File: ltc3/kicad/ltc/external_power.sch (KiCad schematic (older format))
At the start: 46 parts, among them IC701 TLP3542, IC702 TLP3542, IC703 TLP3542, IC704 TLP3542, M701 W28-XQ1A-1, M702 W28-XQ1A-1, M703 W28-XQ1A-1, M704 W28-XQ1A-1, P701 43045-1000, P702 43025-1000, P703 43045-0800, P704 43025-0800, P705 43045-0800, P706 43025-0800, P707 1327G6, P708 1327, P709 1327G6, P710 1327, P711 1327G6, P712 1327, P713 1327G6, P714 1327, Q701 PMV45EN, Q702 PMV45EN, Q703 PMV45EN, Q704 PMV45EN, SW701 SP3T, SW702 SP3T, SW703 SP3T, SW704 SP3T

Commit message: LTC3: Split single-board design into two boards.
Separated the charge controller and cell protection circuitry onto its
own board (kicad/charge_controller).  The DC-DC converters,
BeagleBone, external power and triggers, and ignition fire control
circuitry remains together (kicad/ltc).

Both boards have had their schematics updated.  Sub-sheets for
circuitry moved to the other board were removed.  Still more work
remaining, though (e.g., add I2C connectors to Charge Controller
schematic; add battery power connector to LTC board; etc.).

Schematic components were *not* re-annotated to align with new sheet
numbering, as it would screw up the existing layout work (i.e., placed
components would disappear), and that would make us sad engineers.

Both boards have had their PCB layouts converted to four-layer.
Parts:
- M701, M702, M703, M704, P702, P704, P706, P707, P708, P709, P710, P711, P712, P713, P714, SW701, SW702, SW703, SW704: footprint OFF-BOARD -> (none)
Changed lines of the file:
@@
 LIBS:atmel
 LIBS:audio
-LIBS:bbd
 LIBS:brooktre
 LIBS:cmos4000
@@
 LIBS:transistors
 LIBS:ttl_ieee
-LIBS:Launch_Tower_Computer_III-cache
 EELAYER 25 0
 EELAYER END
 $Descr B 17000 11000
 encoding utf-8
-Sheet 7 8
+Sheet 7 6
 Title "LTC3 External Device Power"
 Date "2016-05-09"
@@
 EXT_PWR_EN_1
 $Comp
-L GND #PWR701
+L GND #PWR081
 U 1 1 557E02AD
 P 1650 4100
-F 0 "#PWR701" H 1650 4100 30  0001 C CNN
+F 0 "#PWR081" H 1650 4100 30  0001 C CNN
 F 1 "GND" H 1650 4030 30  0001 C CNN
 F 2 "" H 1650 4100 60  0000 C CNN
@@
 $EndComp
 $Comp
-L GND #PWR705
+L GND #PWR082
 U 1 1 557E02DD
 P 3900 3800
-F 0 "#PWR705" H 3900 3800 30  0001 C CNN
+F 0 "#PWR082" H 3900 3800 30  0001 C CNN
 F 1 "GND" H 3900 3730 30  0001 C CNN
 F 2 "" H 3900 3800 60  0000 C CNN
@@
 $EndComp
 $Comp
-L +5V #PWR703
+L +5V #PWR083
 U 1 1 56544A2B
 P 2450 2250
-F 0 "#PWR703" H 2450 2100 50  0001 C CNN
+F 0 "#PWR083" H 2450 2100 50  0001 C CNN
 F 1 "+5V" H 2450 2390 50  0000 C CNN
 F 2 "" H 2450 2250 60  0000 C CNN
@@
 EXT_PWR_EN_2
 $Comp
-L GND #PWR707
+L GND #PWR084
 U 1 1 56CA75BB
 P 6850 4100
-F 0 "#PWR707" H 6850 4100 30  0001 C CNN
+F 0 "#PWR084" H 6850 4100 30  0001 C CNN
 F 1 "GND" H 6850 4030 30  0001 C CNN
 F 2 "" H 6850 4100 60  0000 C CNN
@@
 $EndComp
 $Comp
-L GND #PWR711
+L GND #PWR085
 U 1 1 56CA75CD
 P 9100 3800
-F 0 "#PWR711" H 9100 3800 30  0001 C CNN
+F 0 "#PWR085" H 9100 3800 30  0001 C CNN
 F 1 "GND" H 9100 3730 30  0001 C CNN
 F 2 "" H 9100 3800 60  0000 C CNN
@@
 $EndComp
 $Comp
-L +5V #PWR709
+L +5V #PWR086
 U 1 1 56CA760C
 P 7650 2250
-F 0 "#PWR709" H 7650 2100 50  0001 C CNN
+F 0 "#PWR086" H 7650 2100 50  0001 C CNN
 F 1 "+5V" H 7650 2390 50  0000 C CNN
 F 2 "" H 7650 2250 60  0000 C CNN
@@
 $EndComp
 $Comp
-L +12V #PWR714
+L +12V #PWR087
 U 1 1 56CA7612
 P 12500 4150
-F 0 "#PWR714" H 12500 4000 50  0001 C CNN
+F 0 "#PWR087" H 12500 4000 50  0001 C CNN
 F 1 "+12V" H 12500 4290 50  0000 C CNN
 F 2 "" H 12500 4150 60  0000 C CNN
@@
 EXT_PWR_EN_3
 $Comp
-L GND #PWR702
+L GND #PWR088
 U 1 1 56CA9336
 P 1650 10100
-F 0 "#PWR702" H 1650 10100 30  0001 C CNN
+F 0 "#PWR088" H 1650 10100 30  0001 C CNN
 F 1 "GND" H 1650 10030 30  0001 C CNN
 F 2 "" H 1650 10100 60  0000 C CNN
@@
 $EndComp
 $Comp
-L +5V #PWR704
+L +5V #PWR089
 U 1 1 56CA9387
 P 2450 8250
-F 0 "#PWR704" H 2450 8100 50  0001 C CNN
+F 0 "#PWR089" H 2450 8100 50  0001 C CNN
 F 1 "+5V" H 2450 8390 50  0000 C CNN
 F 2 "" H 2450 8250 60  0000 C CNN
@@
 EXT_PWR_EN_4
 $Comp
-L GND #PWR708
+L GND #PWR090
 U 1 1 56CA93AD
 P 6850 10100
-F 0 "#PWR708" H 6850 10100 30  0001 C CNN
+F 0 "#PWR090" H 6850 10100 30  0001 C CNN
 F 1 "GND" H 6850 10030 30  0001 C CNN
 F 2 "" H 6850 10100 60  0000 C CNN
@@
 $EndComp
 $Comp
-L GND #PWR712
+L GND #PWR091
 U 1 1 56CA93BF
 P 9100 9800
-F 0 "#PWR712" H 9100 9800 30  0001 C CNN
+F 0 "#PWR091" H 9100 9800 30  0001 C CNN
 F 1 "GND" H 9100 9730 30  0001 C CNN
 F 2 "" H 9100 9800 60  0000 C CNN
@@
 $EndComp
 $Comp
-L +5V #PWR710
+L +5V #PWR092
 U 1 1 56CA93FE
 P 7650 8250
-F 0 "#PWR710" H 7650 8100 50  0001 C CNN
+F 0 "#PWR092" H 7650 8100 50  0001 C CNN
 F 1 "+5V" H 7650 8390 50  0000 C CNN
 F 2 "" H 7650 8250 60  0000 C CNN
@@
 F 0 "P706" H 13700 5150 50  0000 L CNN
 F 1 "43025-0800" V 13800 4250 50  0000 L CNN
-F 2 "OFF-BOARD" H 13700 4650 50  0001 C CNN
+F 2 "" H 13700 4650 50  0001 C CNN
 F 3 "" H 13700 4650 50  0000 C CNN
 F 4 "MicroFit3 2x4 recept." V 13900 4650 50  0000 C CNN "Note"
@@
 F 0 "M703" H 15450 5425 50  0000 C CNN
 F 1 "W28-XQ1A-1" H 15450 5225 50  0000 C CNN
-F 2 "OFF-BOARD" H 15450 5300 50  0001 C CNN
+F 2 "" H 15450 5300 50  0001 C CNN
 F 3 "" H 15450 5300 50  0000 C CNN
 	1    15450 5300
@@
 F 0 "M704" H 15850 5425 50  0000 C CNN
 F 1 "W28-XQ1A-1" H 15850 5225 50  0000 C CNN
-F 2 "OFF-BOARD" H 15850 5300 50  0001 C CNN
+F 2 "" H 15850 5300 50  0001 C CNN
 F 3 "" H 15850 5300 50  0000 C CNN
 	1    15850 5300
@@
 F 0 "M701" H 14650 5425 50  0000 C CNN
 F 1 "W28-XQ1A-1" H 14650 5225 50  0000 C CNN
-F 2 "OFF-BOARD" H 14650 5300 50  0001 C CNN
+F 2 "" H 14650 5300 50  0001 C CNN
 F 3 "" H 14650 5300 50  0000 C CNN
 	1    14650 5300
@@
 F 0 "M702" H 15050 5425 50  0000 C CNN
 F 1 "W28-XQ1A-1" H 15050 5225 50  0000 C CNN
-F 2 "OFF-BOARD" H 15050 5300 50  0001 C CNN
+F 2 "" H 15050 5300 50  0001 C CNN
 F 3 "" H 15050 5300 50  0000 C CNN
 	1    15050 5300
@@
 Manual Override Switches, Front Panel
 $Comp
-L GND #PWR713
+L GND #PWR093
 U 1 1 56DB5084
 P 11800 2200
-F 0 "#PWR713" H 11800 1950 50  0001 C CNN
+F 0 "#PWR093" H 11800 1950 50  0001 C CNN
 F 1 "GND" H 11808 2026 50  0001 C CNN
 F 2 "" H 11800 2200 50  0000 C CNN
@@
 F 0 "SW701" V 13650 2250 50  0000 R CNN
 F 1 "SP3T" V 13750 2250 50  0000 R CNN
-F 2 "OFF-BOARD" H 13125 2475 50  0001 C CNN
+F 2 "" H 13125 2475 50  0001 C CNN
 F 3 "" H 13125 2475 50  0000 C CNN
 	1    13750 2300
@@
 F 0 "P702" H 13000 2150 50  0000 L CNN
 F 1 "43025-1000" V 13100 1100 50  0000 L CNN
-F 2 "OFF-BOARD" H 13000 1600 50  0001 C CNN
+F 2 "" H 13000 1600 50  0001 C CNN
 F 3 "" H 13000 1600 50  0000 C CNN
 F 4 "MicroFit3 2x5 recept." V 13200 1100 50  0000 L CNN "Note"
@@
 F 0 "SW702" V 14300 2250 50  0000 R CNN
 F 1 "SP3T" V 14400 2250 50  0000 R CNN
-F 2 "OFF-BOARD" H 13775 2475 50  0001 C CNN
+F 2 "" H 13775 2475 50  0001 C CNN
 F 3 "" H 13775 2475 50  0000 C CNN
 	1    14400 2300
@@
 F 0 "SW703" V 14950 2250 50  0000 R CNN
 F 1 "SP3T" V 15050 2250 50  0000 R CNN
-F 2 "OFF-BOARD" H 14425 2475 50  0001 C CNN
+F 2 "" H 14425 2475 50  0001 C CNN
 F 3 "" H 14425 2475 50  0000 C CNN
 	1    15050 2300
@@
 F 0 "SW704" V 15600 2250 50  0000 R CNN
 F 1 "SP3T" V 15700 2250 50  0000 R CNN
-F 2 "OFF-BOARD" H 15075 2475 50  0001 C CNN
+F 2 "" H 15075 2475 50  0001 C CNN
 F 3 "" H 15075 2475 50  0000 C CNN
 	1    15700 2300
@@
 F 0 "P704" H 13950 7850 50  0000 L CNN
 F 1 "43025-0800" V 14050 6950 50  0000 L CNN
-F 2 "OFF-BOARD" H 13950 7350 50  0001 C CNN
+F 2 "" H 13950 7350 50  0001 C CNN
 F 3 "" H 13950 7350 50  0000 C CNN
 F 4 "MicroFit3 2x4 recept." V 14150 7350 50  0000 C CNN "Note"
@@
 $EndComp
 $Comp
-L GND #PWR715
+L GND #PWR094
 U 1 1 57141ACA
 P 12850 7850
-F 0 "#PWR715" H 12850 7600 50  0001 C CNN
+F 0 "#PWR094" H 12850 7600 50  0001 C CNN
 F 1 "GND" H 12858 7677 50  0000 C CNN
 F 2 "" H 12850 7850 50  0000 C CNN
@@
 $EndComp
 $Comp
-L GND #PWR706
+L GND #PWR095
 U 1 1 57147239
 P 3900 9800
-F 0 "#PWR706" H 3900 9550 50  0001 C CNN
+F 0 "#PWR095" H 3900 9550 50  0001 C CNN
 F 1 "GND" H 3908 9627 50  0000 C CNN
 F 2 "" H 3900 9800 50  0000 C CNN
@@
 F 0 "P707" H 14750 8150 50  0000 L CNN
 F 1 "1327G6" H 14900 8150 50  0001 C CNN
-F 2 "OFF-BOARD" H 14650 8150 50  0001 C CNN
+F 2 "" H 14650 8150 50  0001 C CNN
 F 3 "" H 14650 8150 50  0000 C CNN
 	1    14650 8150
@@
 F 0 "P708" H 14900 8150 50  0000 L CNN
 F 1 "1327" H 15000 8200 50  0001 C CNN
-F 2 "OFF-BOARD" H 14800 8150 50  0001 C CNN
+F 2 "" H 14800 8150 50  0001 C CNN
 F 3 "" H 14800 8150 50  0000 C CNN
 	1    14800 8150
@@
 F 0 "P709" H 15150 8150 50  0000 L CNN
 F 1 "1327G6" H 15300 8150 50  0001 C CNN
-F 2 "OFF-BOARD" H 15050 8150 50  0001 C CNN
+F 2 "" H 15050 8150 50  0001 C CNN
 F 3 "" H 15050 8150 50  0000 C CNN
 	1    15050 8150
@@
 F 0 "P710" H 15300 8150 50  0000 L CNN
 F 1 "1327" H 15450 8250 50  0001 C CNN
-F 2 "OFF-BOARD" H 15200 8150 50  0001 C CNN
+F 2 "" H 15200 8150 50  0001 C CNN
 F 3 "" H 15200 8150 50  0000 C CNN
 	1    15200 8150
@@
 F 0 "P711" H 15550 8150 50  0000 L CNN
 F 1 "1327G6" H 15800 8150 50  0001 C CNN
-F 2 "OFF-BOARD" H 15450 8150 50  0001 C CNN
+F 2 "" H 15450 8150 50  0001 C CNN
 F 3 "" H 15450 8150 50  0000 C CNN
 	1    15450 8150
@@
 F 0 "P712" H 15700 8150 50  0000 L CNN
 F 1 "1327" H 15900 8150 50  0001 C CNN
-F 2 "OFF-BOARD" H 15600 8150 50  0001 C CNN
+F 2 "" H 15600 8150 50  0001 C CNN
 F 3 "" H 15600 8150 50  0000 C CNN
 	1    15600 8150
@@
 F 0 "P713" H 15950 8150 50  0000 L CNN
 F 1 "1327G6" H 16200 8150 50  0001 C CNN
-F 2 "OFF-BOARD" H 15850 8150 50  0001 C CNN
+F 2 "" H 15850 8150 50  0001 C CNN
 F 3 "" H 15850 8150 50  0000 C CNN
 	1    15850 8150
@@
 F 0 "P714" H 16100 8150 50  0000 L CNN
 F 1 "1327" H 16300 8150 50  0001 C CNN
-F 2 "OFF-BOARD" H 16000 8150 50  0001 C CNN
+F 2 "" H 16000 8150 50  0001 C CNN
 F 3 "" H 16000 8150 50  0000 C CNN
 	1    16000 8150

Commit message: LTC3: Updates to LTC schematic.
1. Cleaned up top-level sheet.
2. Added board-to-board connectors for power, I2C.
3. Miscelleneous component part selection/changes.
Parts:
- removed C702, C703, C704: 1μ, Capacitors_SMD:C_0805, symbol C
- removed IC701, IC702, IC703, IC704: TLP3542, Housings_DIP:DIP-6_W7.62mm, symbol TLP3542
- removed M702, M703, M704: W28-XQ1A-1, symbol BREAKER_1P
- removed P701: 43045-1000, Connectors_Molex:Molex_Microfit3_Header_02x05_Angled_43045-100x, symbol CONN_01X10
- removed P702: 43025-1000, symbol CONN_01X10
- removed P703: 43045-0800, Connectors_Molex:Molex_Microfit3_Header_02x04_Angled_43045-080x, symbol CONN_01X08
- removed P704: 43025-0800, symbol CONN_01X08
- removed P709, P711, P713: 1327G6, symbol CONN_01X01
- removed P710, P712, P714: 1327, symbol CONN_01X01
- removed Q702, Q703, Q704: PMV45EN, TO_SOT_Packages_SMD:SOT-23, symbol PMV45EN
- added C502, C503, C504: 1μ, Capacitors_SMD:C_0805, symbol C
- added M502, M503, M504: 1A, symbol BREAKER_1P
- added P501: JST PH header, Connectors_JST:JST_PH_B9B-PH-K_09x2.00mm_Straight, symbol CONN_01X09
- added P502: JST PH housing, ~, symbol CONN_01X09
- added P505: MicroFit header, Connectors_Molex:Molex_Microfit3_Header_02x04_Angled_43045-080x, symbol CONN_01X08
- added P506: MicroFit recept., symbol CONN_01X08
- added P509, P510, P511, P512, P513, P514: PowerPole, symbol CONN_01X01
- added Q502, Q503, Q504: PMV45EN, TO_SOT_Packages_SMD:SOT-23, symbol PMV45EN
- added U501, U502, U503, U504: TLP3542, Housings_DIP:DIP-6_W7.62mm, symbol TLP3542
- C501: renamed from C701; Mfg_Name (none) -> -; Mfg_PN (none) -> -; Note (none) -> -; Spec (none) -> 25V
- M501: renamed from M701; value W28-XQ1A-1 -> 1A; Mfg_Name (none) -> TE; Mfg_PN (none) -> W28-XQ1A-1; Note (none) -> -; Spec (none) -> -
- P503: renamed from P705; value 43045-0800 -> MicroFit header; Mfg_Name (none) -> Molex; Mfg_PN (none) -> 43045-0800; Note MicroFit3 2x4 header -> -
- P504: renamed from P706; value 43025-0800 -> MicroFit recept.; Mfg_Name (none) -> Molex; Mfg_PN (none) -> 43025-0800; Note MicroFit3 2x4 recept. -> -
- P507: renamed from P707; value 1327G6 -> PowerPole; Mfg_Name (none) -> Anderson; Mfg_PN (none) -> 1327G6; Note (none) -> -
- P508: renamed from P708; value 1327 -> PowerPole; Mfg_Name (none) -> Anderson; Mfg_PN (none) -> 1327; Note (none) -> -
- Q501: renamed from Q701; Mfg_Name (none) -> NXP; Mfg_PN (none) -> PMV45EN; Note (none) -> -; Spec (none) -> -
- R501: renamed from R701; Mfg_Name (none) -> -; Mfg_PN (none) -> -; Note (none) -> -; Spec (none) -> -
- R503: renamed from R703; Mfg_Name (none) -> -; Mfg_PN (none) -> -; Note (none) -> -; Spec (none) -> -
- R505: renamed from R705; Mfg_Name (none) -> -; Mfg_PN (none) -> -; Note (none) -> -; Spec (none) -> -
- renumbered R702 to R502, R704 to R504, R706 to R506, R707 to R507, R708 to R508, R709 to R509, R710 to R510, R711 to R511, R712 to R512, SW701 to SW501, SW702 to SW502, SW703 to SW503, SW704 to SW504
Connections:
- net EXT_POW_1_FET_D: now also P501.1 (P1)
- net EXT_POW_1_LED_CATH: now also P501.2 (P2), U501.2
- net EXT_POW_1_OPTO_RELAY_P: now also U501.6
- net EXT_POW_2_FET_D: now also P501.3 (P3), Q502.3 (D)
- net EXT_POW_2_LED_CATH: now also P501.4 (P4), U502.2
- net EXT_POW_2_OPTO_RELAY_P: now also U502.6
- net EXT_POW_3_FET_D: now also P501.5 (P5), Q503.3 (D)
- net EXT_POW_3_LED_CATH: now also P501.6 (P6), U503.2
- net EXT_POW_3_OPTO_RELAY_P: now also U503.6
- net EXT_POW_4_FET_D: now also P501.7 (P7), Q504.3 (D)
- net EXT_POW_4_LED_CATH: now also P501.8 (P8), U504.2
- net EXT_POW_4_OPTO_RELAY_P: now also U504.6
- net EXT_PWR_EN_2: now also Q502.1 (G)
- net EXT_PWR_EN_3: now also Q503.1 (G)
- net EXT_PWR_EN_4: now also Q504.1 (G)
- net GND: now also C502.2, C503.2, C504.2, P501.9 (P9), P505.2 (P2), P505.4 (P4), P505.6 (P6), P505.8 (P8), Q502.2 (S), Q503.2 (S), Q504.2 (S)
- net EXT_PWR_1_OUT: now reaches C501.1, R503.1
- net EXT_PWR_1_OUT: now also P505.1 (P1), U501.4
- net at R501.2: now also U501.1
- net EXT_PWR_2_OUT: now reaches R504.1
- net EXT_PWR_2_OUT: now also C502.1, P505.3 (P3), U502.4
- net at R502.2: now also U502.1
- net EXT_PWR_3_OUT: now reaches R509.1
- net EXT_PWR_3_OUT: now also C503.1, P505.5 (P5), U503.4
- net at R507.2: now also U503.1
- net EXT_PWR_4_OUT: now reaches R510.1
- net EXT_PWR_4_OUT: now also C504.1, P505.7 (P7), U504.4
- net at R508.2: now also U504.1
- net at P504.5 (P5): now also M503.1
- net at P504.6 (P6): now also M503.2
- net at P504.7 (P7): now also M504.1
- net at P504.8 (P8): now also M504.2
- net at P504.3 (P3): now also M502.1
- net at P504.4 (P4): now also M502.2
- net at SW501.1: now also P502.2 (P2)
- net at SW501.3: now also P502.1 (P1)
- net at SW501.4, SW502.4, SW503.4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: now also P502.9 (P9)
- net at SW502.3: now also P502.3 (P3)
- net at SW502.1: now also P502.4 (P4)
- net at SW503.3: now also P502.5 (P5)
- net at SW503.1: now also P502.6 (P6)
- net at SW504.3: now also P502.7 (P7)
- net at SW504.1: now also P502.8 (P8)
- net at P508.1 (P1): now also P506.7 (P7)
- net at P507.1 (P1): now also P506.8 (P8)
- new net: P506.1 (P1), P514.1 (P1)
- new net: P506.2 (P2), P513.1 (P1)
- new net: P506.3 (P3), P512.1 (P1)
- new net: P506.4 (P4), P511.1 (P1)
- new net: P506.5 (P5), P510.1 (P1)
- new net: P506.6 (P6), P509.1 (P1)
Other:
- note removed: "12V: 1327 (red)\ngnd: 1327G6 (black)"
- moved on the sheet: P507, P508

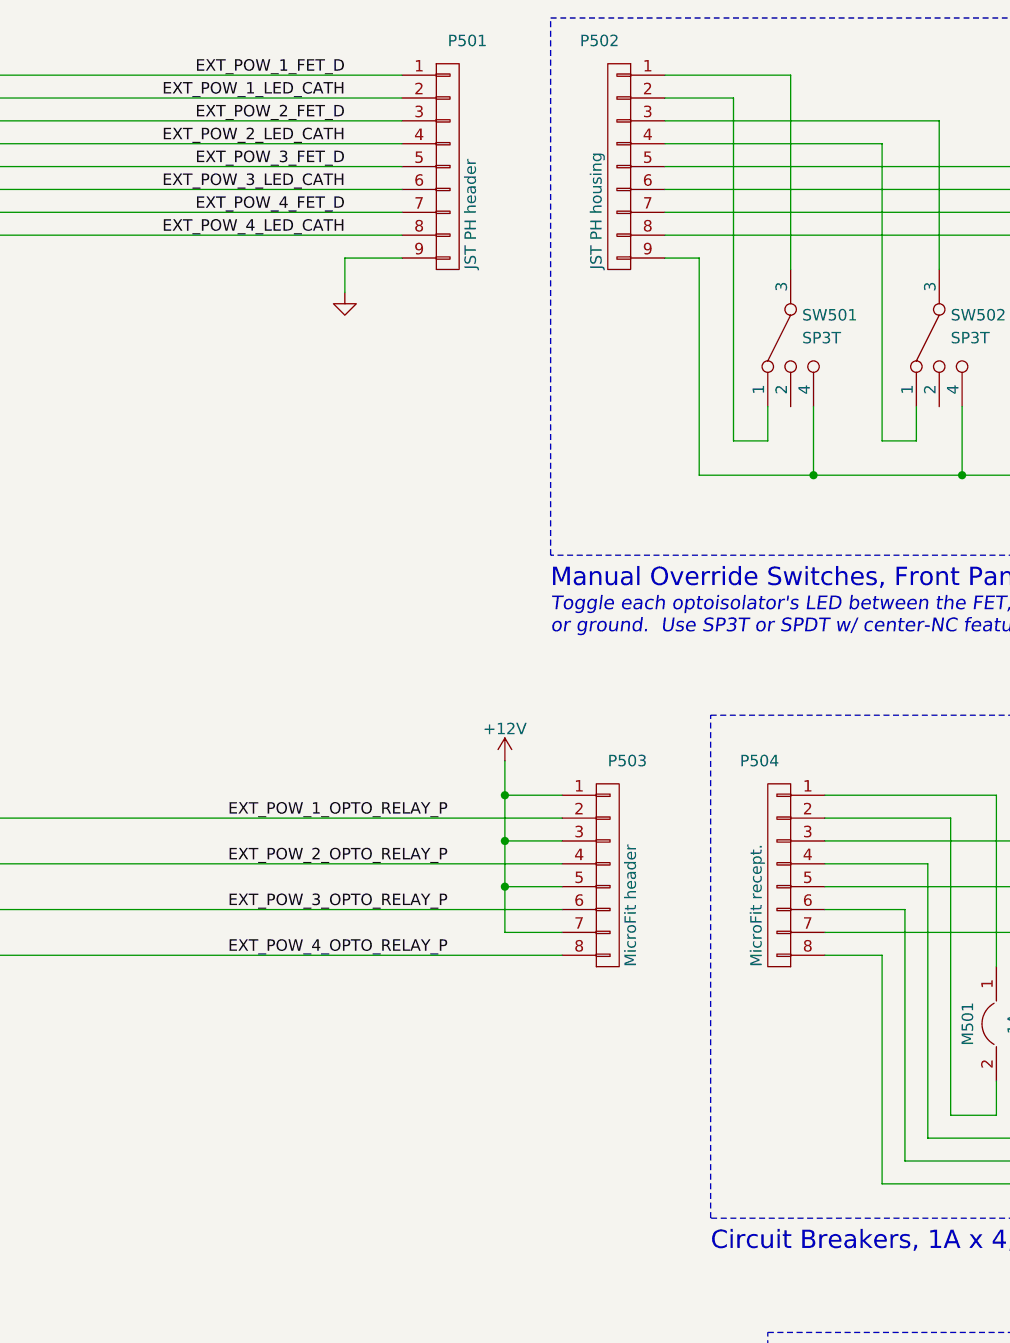
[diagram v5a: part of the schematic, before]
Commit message: LTC3: More BOM work, mostly on the LTC proper.
Plus a few minor tweaks to the charge controller and cell protection
BOMs that should not impact PCB layout.

Nearly finished with LTC BOM.
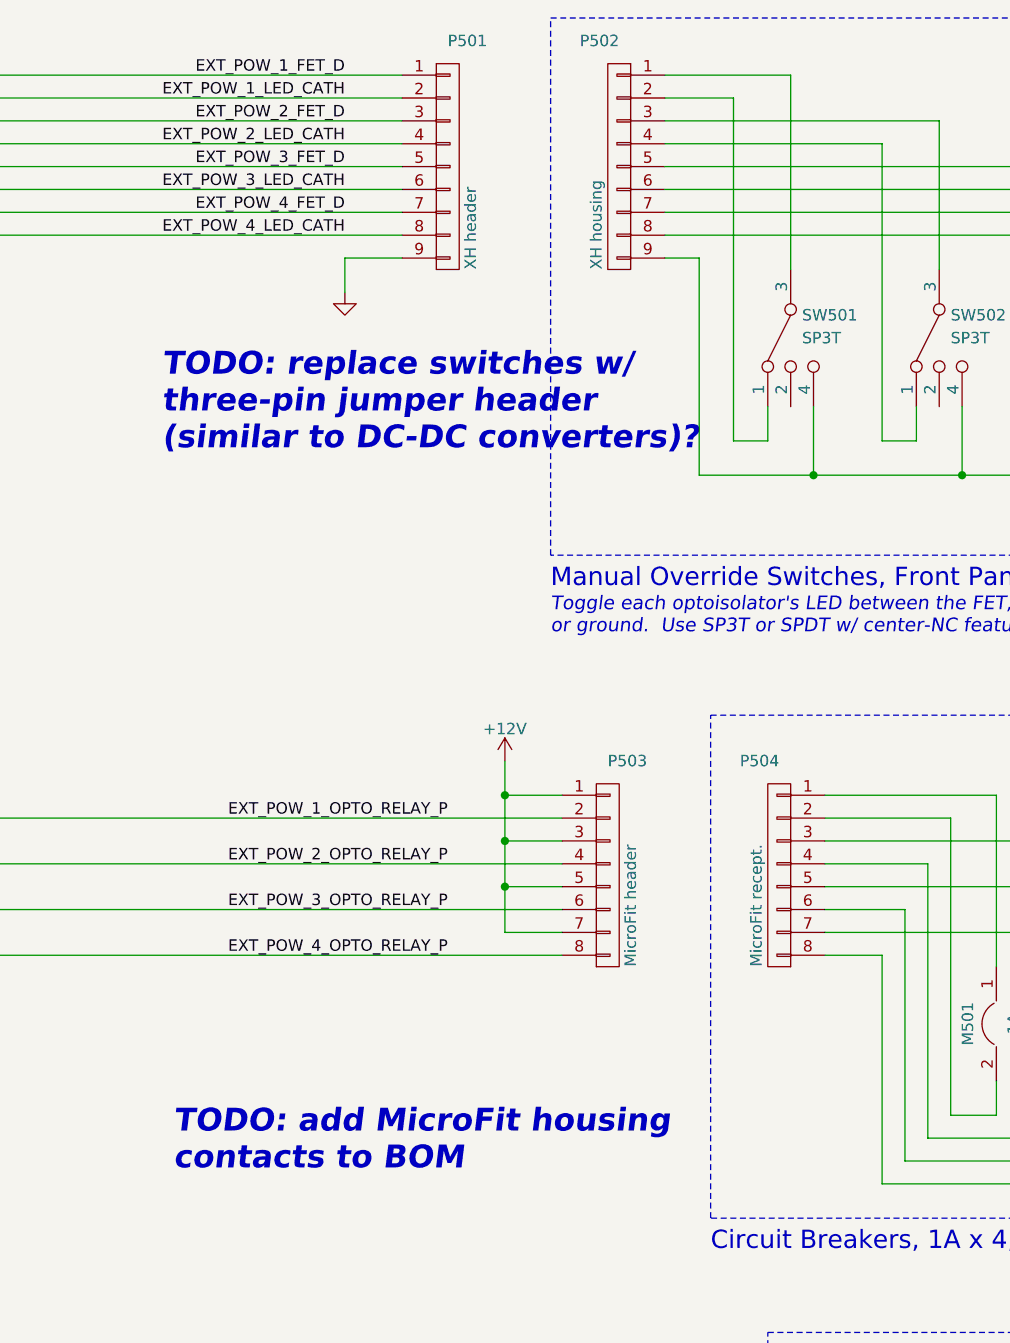
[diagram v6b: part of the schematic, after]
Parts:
- C501, C502, C503, C504: Mfg_Description (none) -> 100V X7S 10%; Mfg_Name - -> TDK; Mfg_PN - -> CGA4J3X7S2A105K125AB
- M501, M502, M503, M504: footprint (none) -> ~; Mfg_Description (none) -> 1A 250VAC 32VDC; Note - -> OFF-BOARD
- P501: value JST PH header -> XH header; footprint Connectors_JST:JST_PH_B9B-PH-K_09x2.00mm_Straight -> -; Mfg_Description (none) -> -; Mfg_PN B9B-PH-K-S -> -; Note (none) -> -; Spec (none) -> -
- P502: value JST PH housing -> XH housing; footprint ~ -> -; Mfg_Description (none) -> -; Mfg_PN PHR-9 -> -; Note (none) -> -; Spec (none) -> -
- P503, P505: Mfg_Description (none) -> -; Spec (none) -> -
- P504, P506, P507, P508, P509, P510, P511, P512, P513, P514: footprint (none) -> ~; Mfg_Description (none) -> -; Spec (none) -> -
- Q501, Q502, Q503, Q504: Mfg_Description (none) -> MOSFET N-CH 30V; Mfg_PN PMV45EN -> PMV45EN2R
- R501: Mfg_Description (none) -> 1% 1/8W; Mfg_Name - -> Yageo; Mfg_PN - -> RC0805FR-07270RL
- R502, R507, R508: Mfg_Description (none) -> 1% 1/8W; Mfg_Name (none) -> Yageo; Mfg_PN (none) -> RC0805FR-07270RL; Note (none) -> -; Spec (none) -> -
- R503: Mfg_Description (none) -> 1% 1/8W; Mfg_Name - -> Yageo; Mfg_PN - -> RC0805FR-0751KL
- R504, R509, R510: Mfg_Description (none) -> 1% 1/8W; Mfg_Name (none) -> Yageo; Mfg_PN (none) -> RC0805FR-0751KL; Note (none) -> -; Spec (none) -> -
- R505: Mfg_Description (none) -> 1% 1/8W; Mfg_Name - -> Yageo; Mfg_PN - -> RC0805FR-0710KL
- R506, R511, R512: Mfg_Description (none) -> 1% 1/8W; Mfg_Name (none) -> Yageo; Mfg_PN (none) -> RC0805FR-0710KL; Note (none) -> -; Spec (none) -> -
- SW501, SW502, SW503, SW504: footprint (none) -> ~; Mfg_Description (none) -> -; Mfg_Name (none) -> -; Mfg_PN (none) -> -; Note (none) -> OFF-BOARD; Spec (none) -> -
- U501, U502, U503, U504: Mfg_Description (none) -> -
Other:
- note added: "TODO: add MicroFit housing\ncontacts to BOM"
- note added: "TODO: replace switches w/\nthree-pin jumper header\n(similar to DC-DC converters)?"
